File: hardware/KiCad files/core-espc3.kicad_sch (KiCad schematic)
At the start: 15 parts, among them J2 Conn_01x04_Pin, U3 TMAG5273A1QDBVR, U4 TMR1208S, U5 THVD1406DR

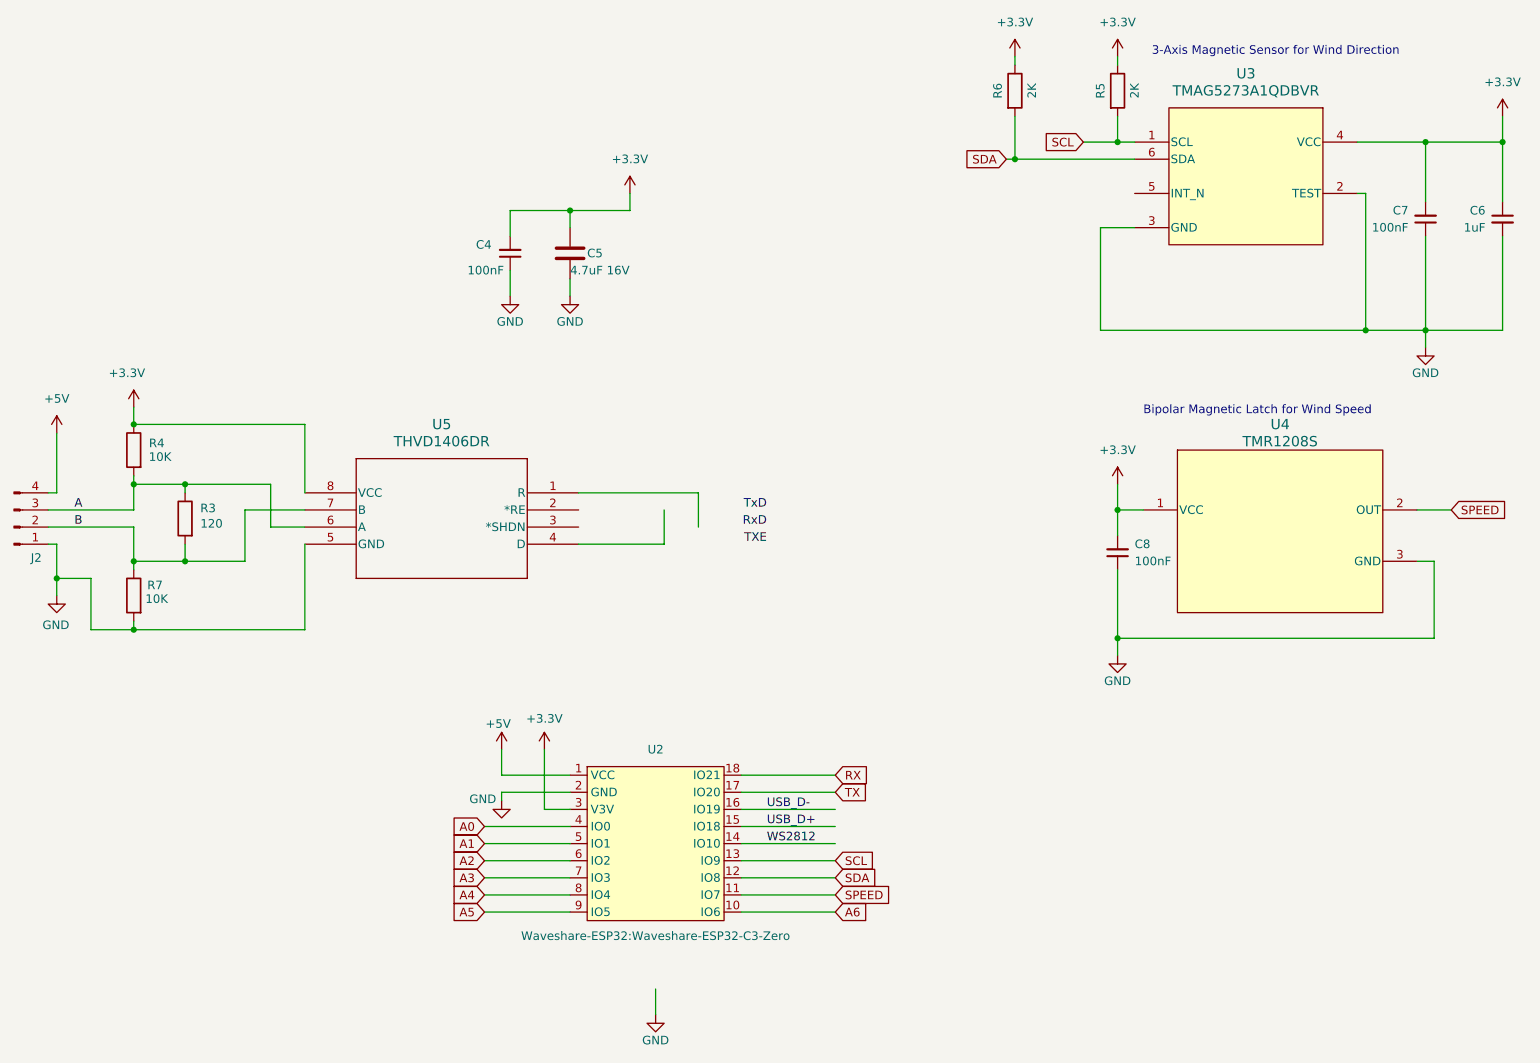
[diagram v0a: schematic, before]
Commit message: Initial PCB Routing Add I2C "expansion" connector for AHT20 + BMP280 sensor
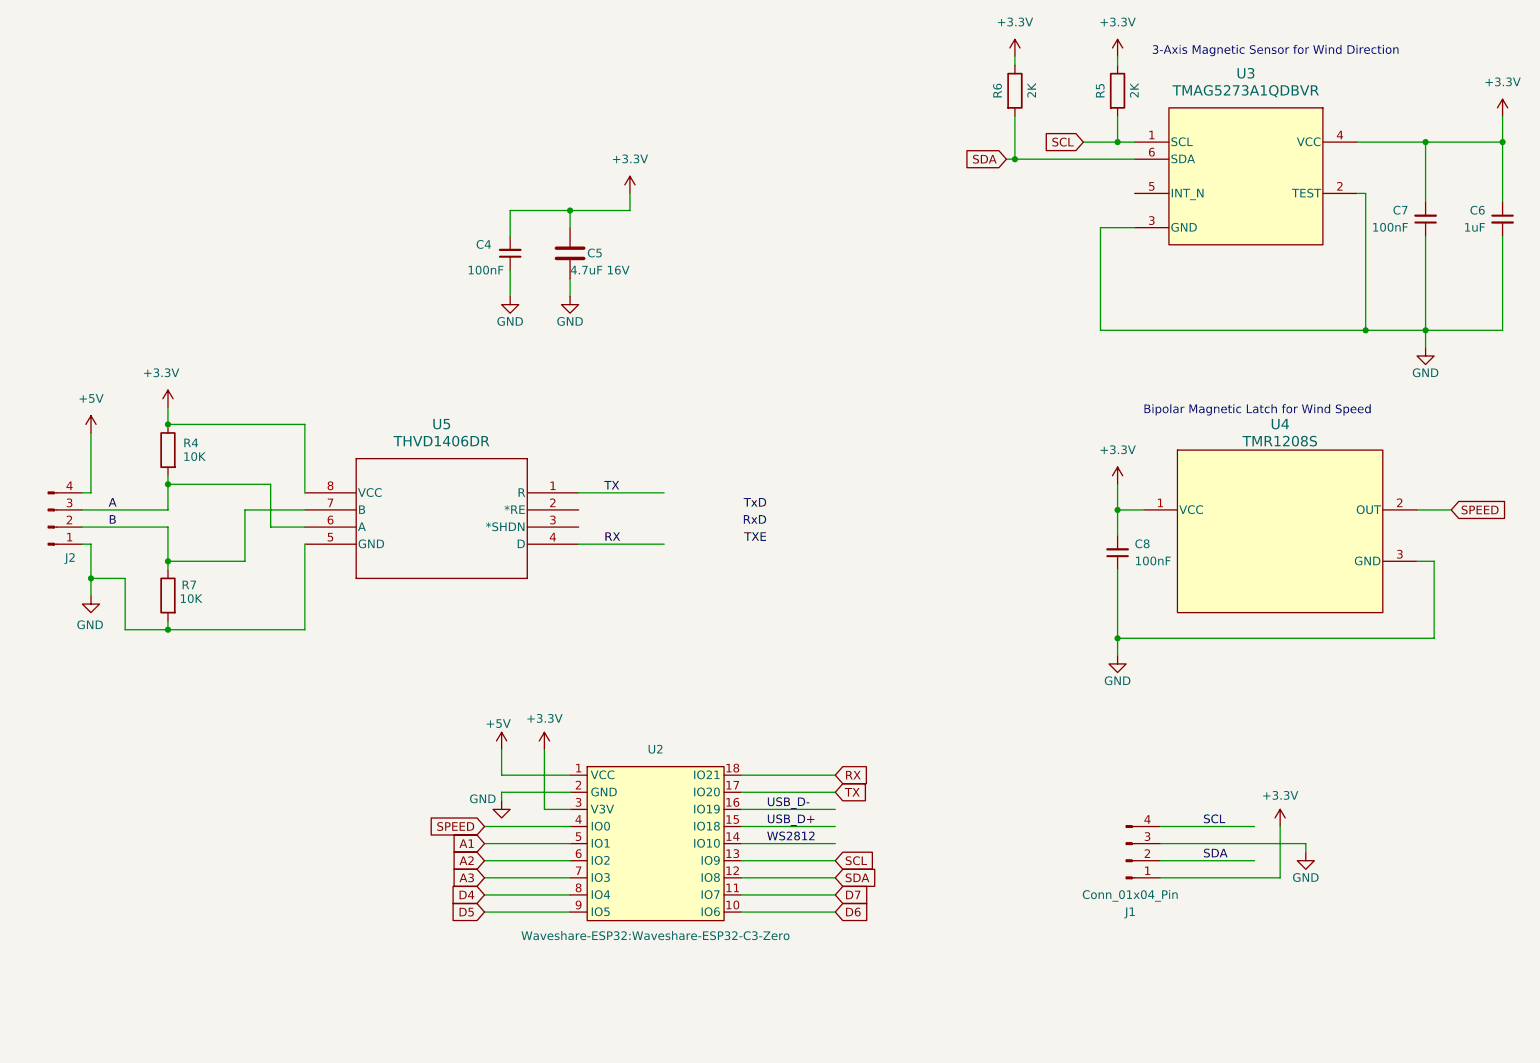
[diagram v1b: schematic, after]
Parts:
- removed R3: 120, Resistor_SMD:R_0603_1608Metric, symbol Device:R
- added J1: Conn_01x04_Pin, Connector_PinHeader_2.54mm:PinHeader_1x04_P2.54mm_Vertical, symbol Connector:Conn_01x04_Pin
- C6, C7, C8: footprint Capacitor_SMD:C_0603_1608Metric -> Capacitor_SMD:C_0603_1608Metric_Pad1.08x0.95mm_HandSolder
- R4, R5, R6, R7: footprint Resistor_SMD:R_0603_1608Metric -> Resistor_SMD:R_0603_1608Metric_Pad0.98x0.95mm_HandSolder
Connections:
- net A0 is gone; now on net SPEED: U2.4 (IO0)
- net +3.3V: now also J1.1 (Pin_1)
- net GND: now also J1.3 (Pin_3)
- net RX: now also U5.4 (D)
- net SCL: now also J1.4 (Pin_4)
- net SDA: now also J1.2 (Pin_2)
- net SPEED: no longer U2.11 (IO7)
- net TX: now also U5.1 (R)
- net A4 renamed D4
- net A5 renamed D5
- net A6 renamed D6
- new net D7: U2.11 (IO7)
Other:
- moved on the sheet: J2, R4, R7
